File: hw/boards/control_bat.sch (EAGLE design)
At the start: 17 parts, among them U1 579-MCP1703T-3002ECB, U2 771-LPC824M201JDH20J, U3 888-XB24CZ7PIS-004

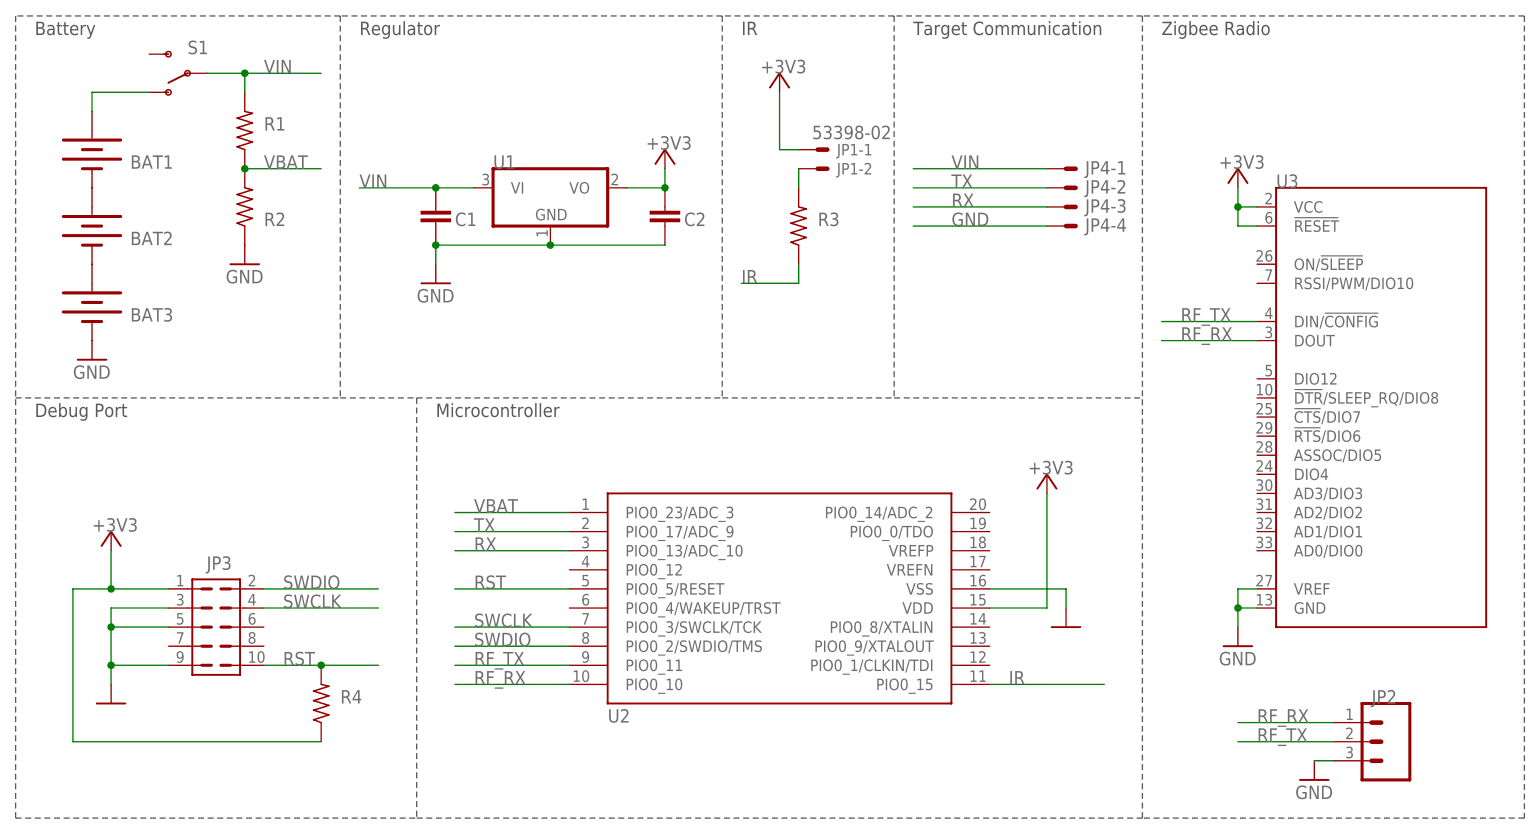
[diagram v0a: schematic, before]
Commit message: Cleanup some routing. Fix some part numbers
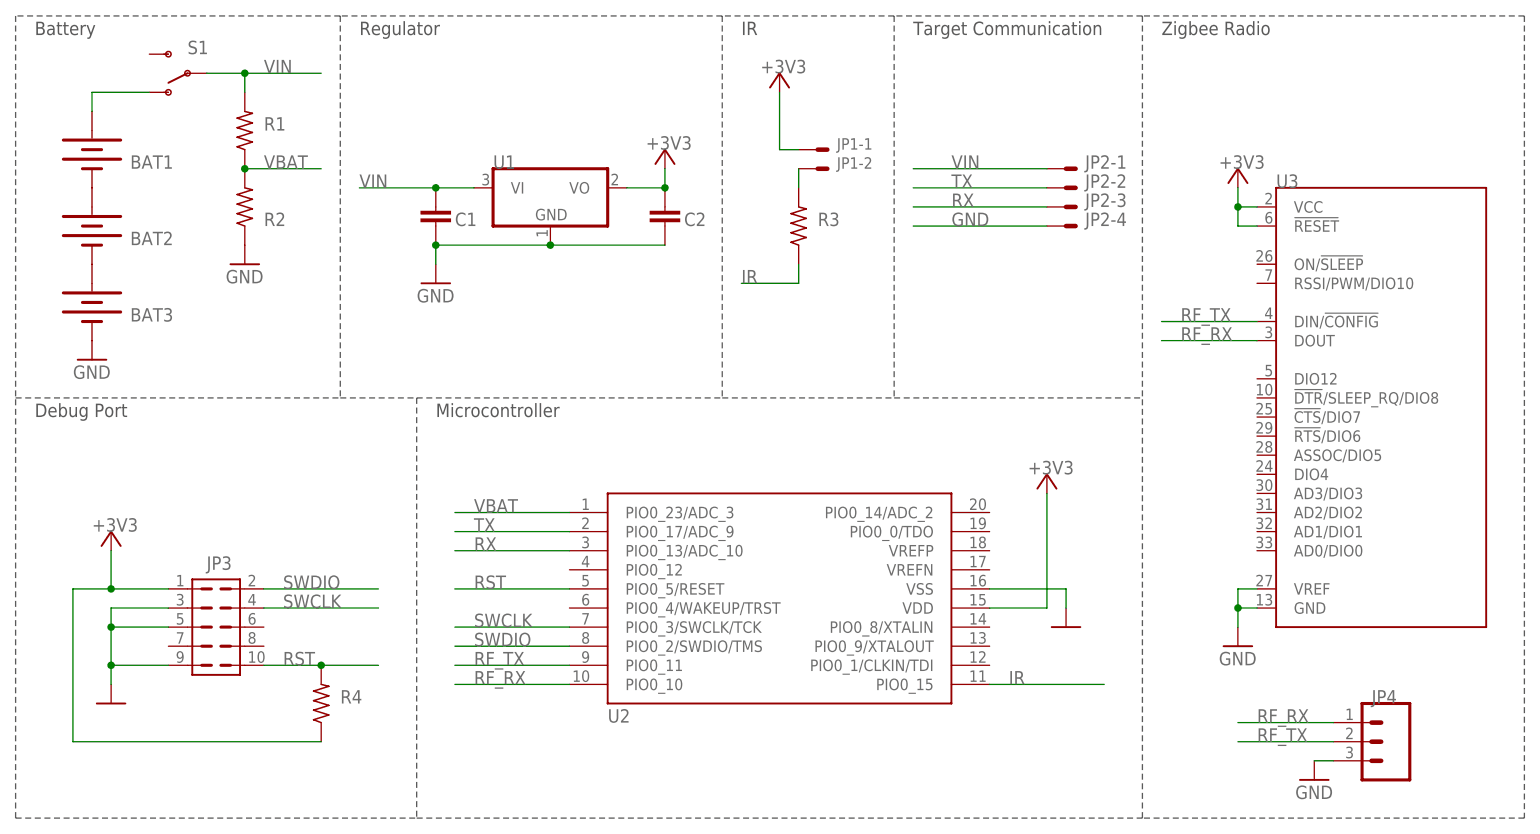
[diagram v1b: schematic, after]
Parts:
- JP1: value 53398-02 -> 798-DF132P125V20
- JP2: value (none) -> 798-DF134P125V20; device SparkFun-Connectors:M03PTH -> con-molex:53398-04
- JP4: value 798-DF134P125V20 -> (none); device con-molex:53398-04 -> SparkFun-Connectors:M03PTH
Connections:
- net GND: now also JP2-4.S, JP4.3; no longer JP2.3, JP4-4.S
- net RF_RX: now also JP4.1; no longer JP2.1
- net RF_TX: now also JP4.2; no longer JP2.2
- net RX: now also JP2-3.S; no longer JP4-3.S
- net TX: now also JP2-2.S; no longer JP4-2.S
- net VIN: now also JP2-1.S; no longer JP4-1.S

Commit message: Cleanup some parts, generate BOM.
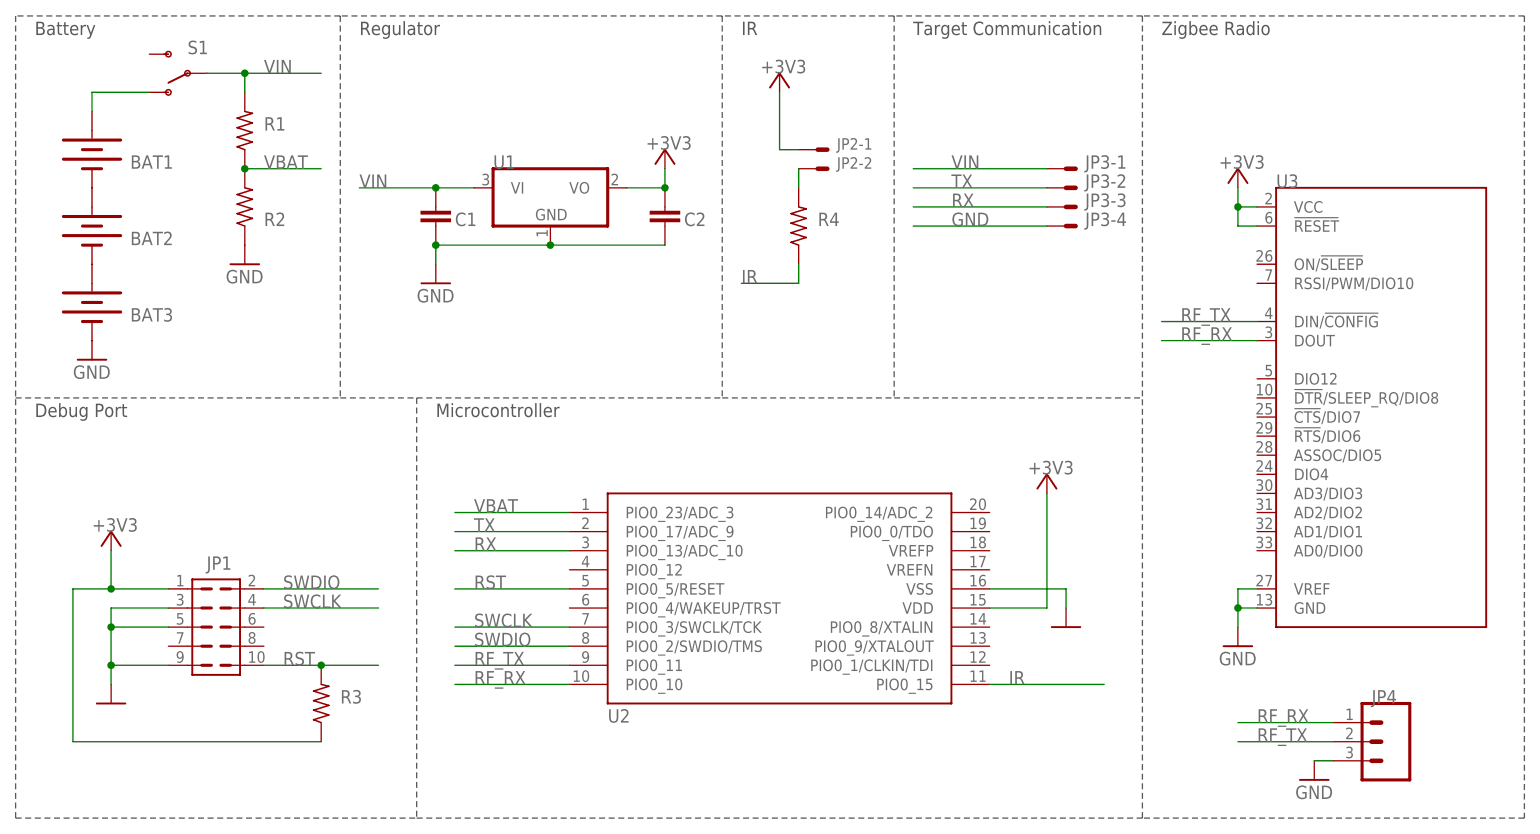
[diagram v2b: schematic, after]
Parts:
- BAT1, BAT2, BAT3: value (none) -> 534-082
- JP1: value 798-DF132P125V20 -> FTSH-105-01-L; device con-molex:53398-02 -> torpedo:FTSH-105
- JP2: value 798-DF134P125V20 -> 798-DF132P125V20; device con-molex:53398-04 -> con-molex:53398-02
- JP3: value FTSH-105-01-L -> 798-DF134P125V20; device torpedo:FTSH-105 -> con-molex:53398-04
- R3: value 71-CRCW0603220RFKEB -> 71-CRCW0603-10K-E3
- R4: value 71-CRCW0603-10K-E3 -> 71-CRCW0603220RFKEB
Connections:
- net +3V3: now also JP1.1, JP2-1.S, R3.1; no longer JP1-1.S, JP3.1, R4.1
- net GND: now also JP1.3, JP1.5, JP1.9, JP3-4.S; no longer JP2-4.S, JP3.3, JP3.5, JP3.9
- net IR: now also R4.1; no longer R3.1
- net N$4: now also JP2-2.S, R4.2; no longer JP1-2.S, R3.2
- net RST: now also JP1.10, R3.2; no longer JP3.10, R4.2
- net RX: now also JP3-3.S; no longer JP2-3.S
- net SWCLK: now also JP1.4; no longer JP3.4
- net SWDIO: now also JP1.2; no longer JP3.2
- net TX: now also JP3-2.S; no longer JP2-2.S
- net VIN: now also JP3-1.S; no longer JP2-1.S
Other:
- moved on the sheet: JP2-1, JP2-2, R3, R4

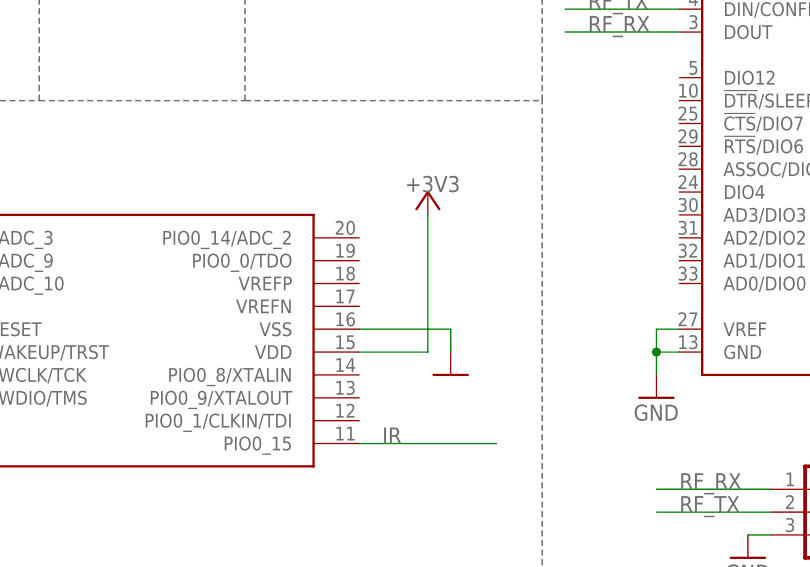
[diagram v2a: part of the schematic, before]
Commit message: Fix adc.
There is no internal reference so I needed to connect the VREFP/VREFN pints to VCC/GND. Added init code to read single adc samples when the voltage-read command is passed.
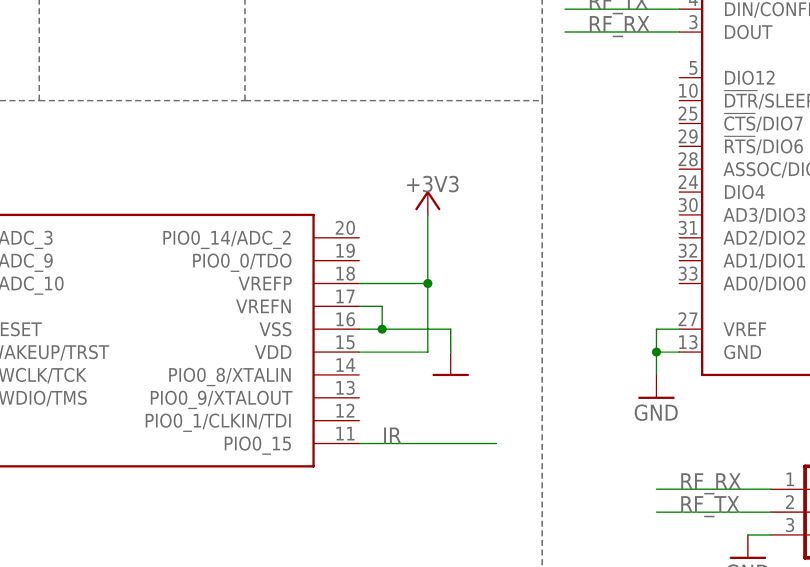
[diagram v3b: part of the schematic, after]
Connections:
- net +3V3: now also U2.VREFP
- net GND: now also U2.VREFN
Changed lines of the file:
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@@
 <segment>
 <pinref part="U2" gate="G$1" pin="VSS"/>
-<wire x1="342.9" y1="33.02" x2="353.06" y2="33.02" width="0.1524" layer="91"/>
+<wire x1="342.9" y1="33.02" x2="345.44" y2="33.02" width="0.1524" layer="91"/>
+<wire x1="345.44" y1="33.02" x2="353.06" y2="33.02" width="0.1524" layer="91"/>
 <wire x1="353.06" y1="33.02" x2="353.06" y2="30.48" width="0.1524" layer="91"/>
 <pinref part="GND5" gate="1" pin="GND"/>
+<pinref part="U2" gate="G$1" pin="VREFN"/>
+<wire x1="342.9" y1="35.56" x2="345.44" y2="35.56" width="0.1524" layer="91"/>
+<wire x1="345.44" y1="35.56" x2="345.44" y2="33.02" width="0.1524" layer="91"/>
+<junction x="345.44" y="33.02"/>
 </segment>
 </net>
@@
 <pinref part="+3V34" gate="G$1" pin="+3V3"/>
 <pinref part="U2" gate="G$1" pin="VDD"/>
-<wire x1="350.52" y1="45.72" x2="350.52" y2="30.48" width="0.1524" layer="91"/>
+<wire x1="350.52" y1="45.72" x2="350.52" y2="38.1" width="0.1524" layer="91"/>
+<wire x1="350.52" y1="38.1" x2="350.52" y2="30.48" width="0.1524" layer="91"/>
 <wire x1="350.52" y1="30.48" x2="342.9" y2="30.48" width="0.1524" layer="91"/>
+<pinref part="U2" gate="G$1" pin="VREFP"/>
+<wire x1="342.9" y1="38.1" x2="350.52" y2="38.1" width="0.1524" layer="91"/>
+<junction x="350.52" y="38.1"/>
 </segment>
 </net>
